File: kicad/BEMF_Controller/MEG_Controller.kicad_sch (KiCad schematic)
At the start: 77 parts, among them J1 HEADER4VALULOK, J2 Recovery, J3 FUSE, J5 Load, J7 Vin, Q1 C3M0280090D, Q2 C3M0280090D, Q3 C3M0280090D, Q4 C3M0280090D, U1 BlackPill_STLINK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

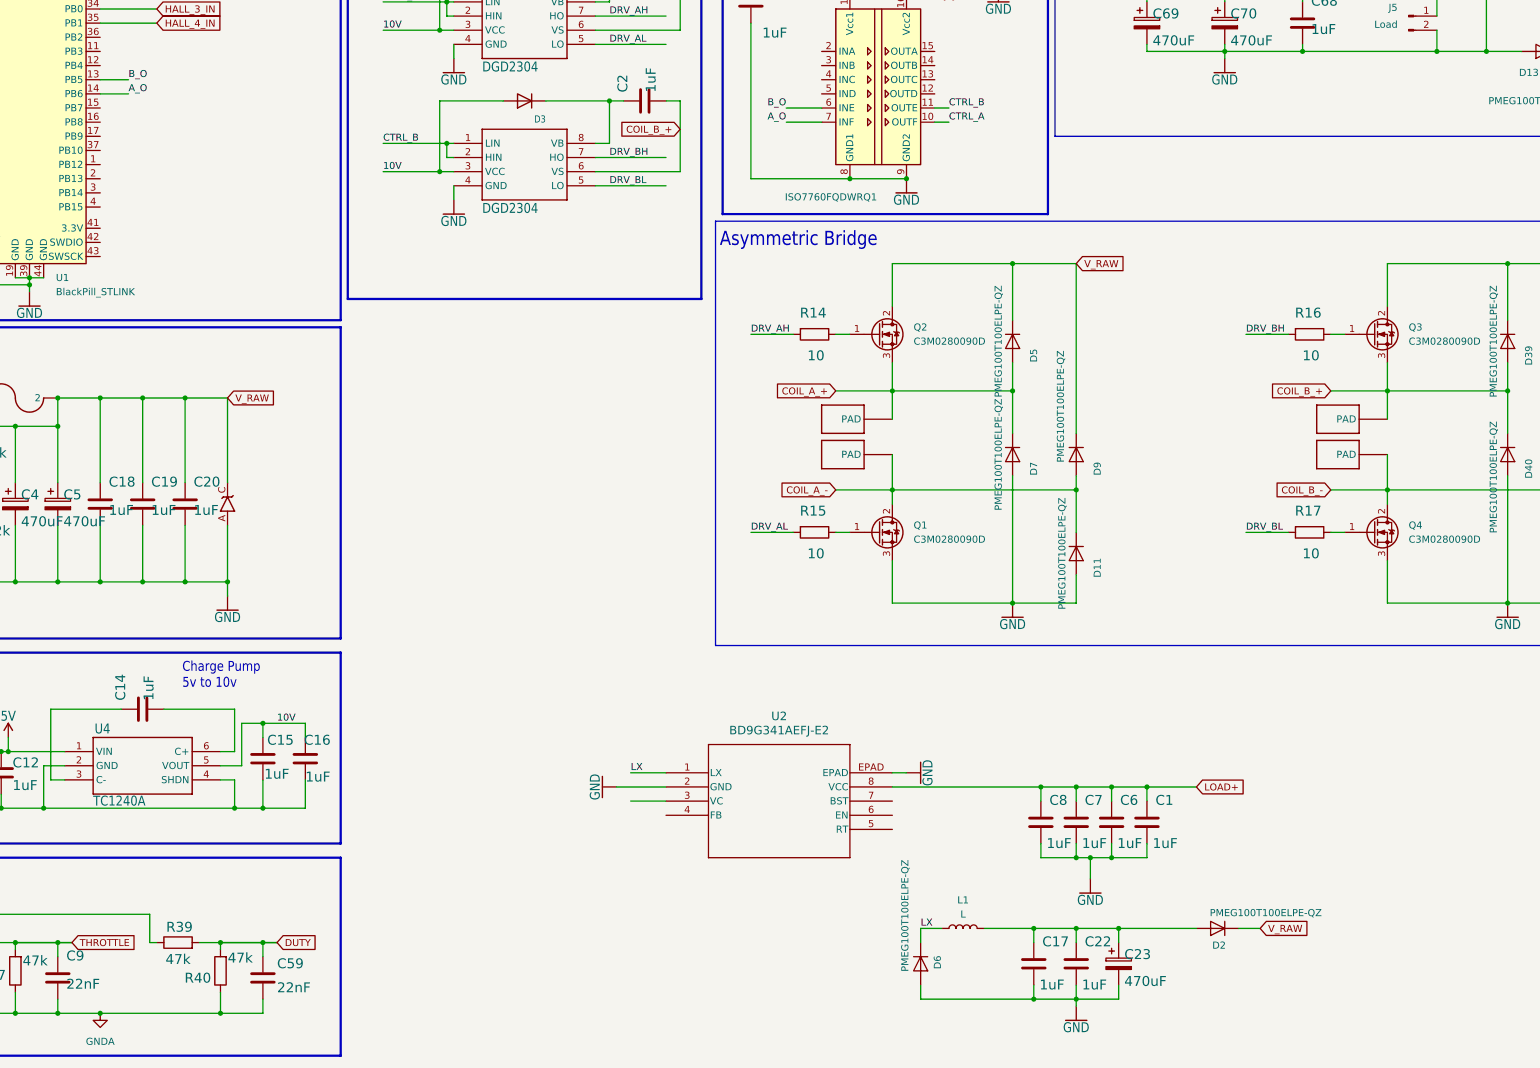
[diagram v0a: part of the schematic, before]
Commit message: Finished buck converter schematic
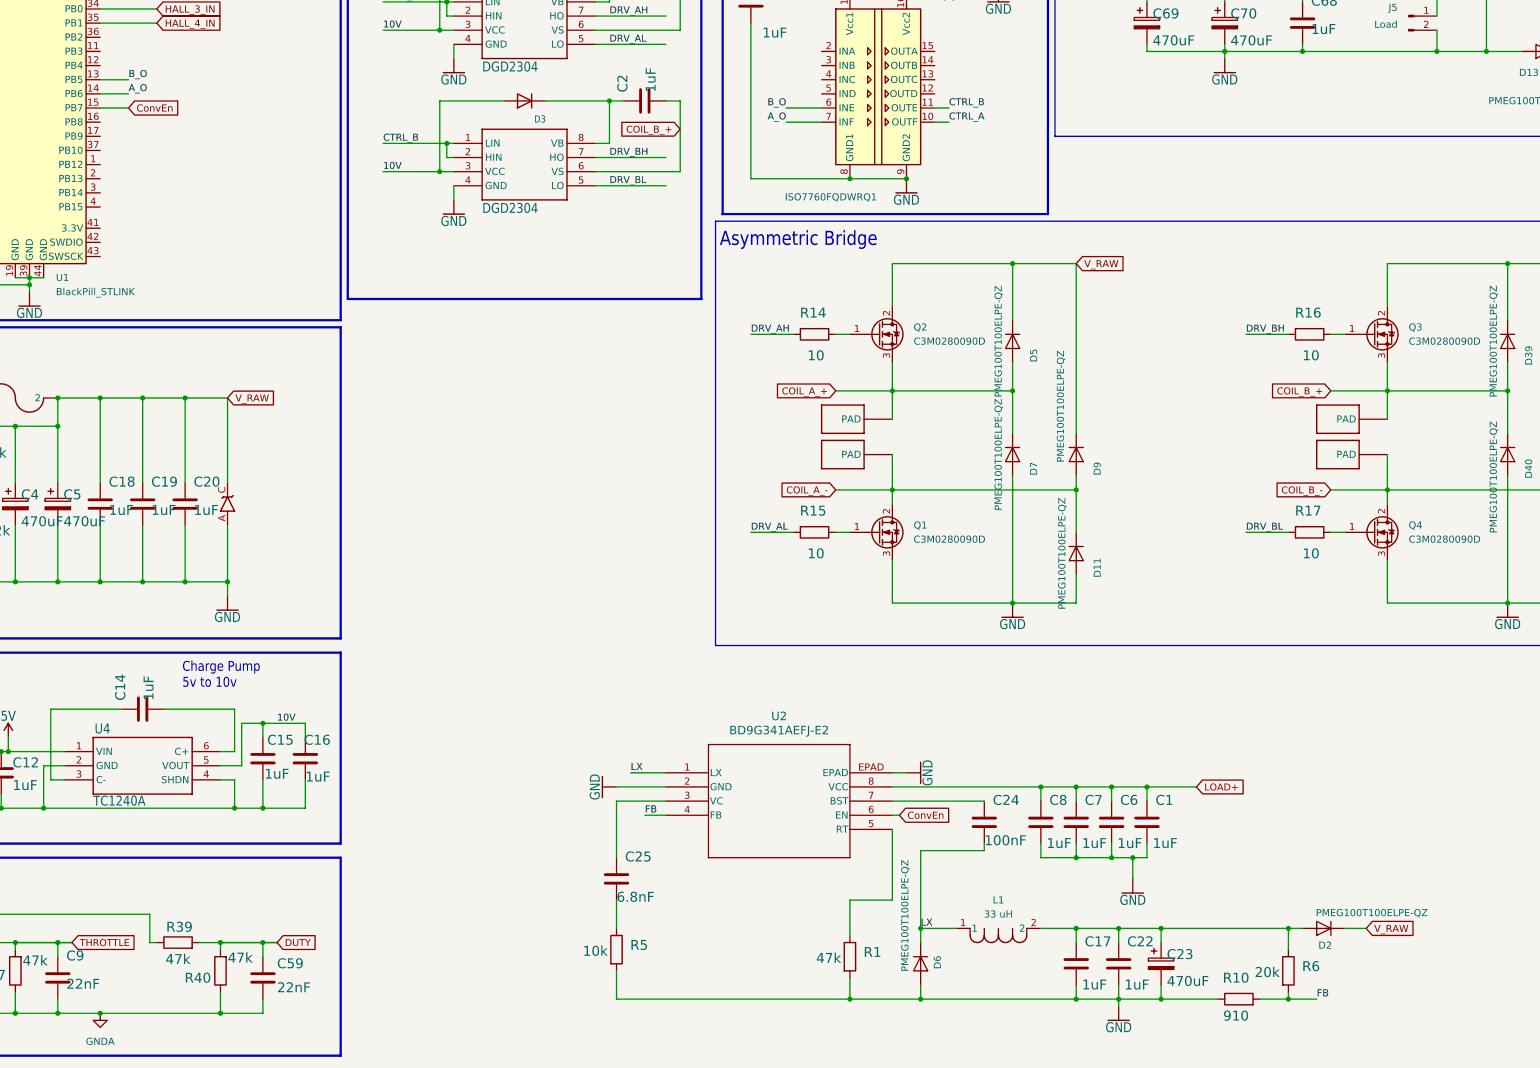
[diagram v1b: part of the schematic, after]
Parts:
- added C24: 100nF, Capacitor_SMD:C_0805_2012Metric, symbol Component_Library:CHV1812N250105MXT
- added C25: 6.8nF, Capacitor_SMD:C_0805_2012Metric, symbol Component_Library:CHV1812N250105MXT
- added R1: 47k, Resistor_SMD:R_1206_3216Metric, symbol Component_Library:R47k
- added R10: 910, Resistor_SMD:R_1206_3216Metric, symbol Component_Library:R47k
- added R5: 10k, Resistor_SMD:R_1206_3216Metric, symbol Component_Library:R47k
- added R6: 20k, Resistor_SMD:R_1206_3216Metric, symbol Component_Library:R47k
- L1: value L -> 33 uH; footprint (none) -> main:IND_BOURNS_SRN1060; symbol Device:L -> Component_Library:33 uH SRN1060-330M
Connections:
- net GND: now also R1.2, R10.1, R5.2
- net LX: now also C24.2
- net at C17.1, C22.1, C23.1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: now also R6.1
- net at U2.3 (VC): now also C25.1
- net FB: now reaches U2.4 (FB)
- net FB: now also R10.2, R6.2
- net at U2.5 (RT): now also R1.1
- net ConvEn: now reaches U2.6 (EN)
- net ConvEn: now also U1.15 (PB7)
- net at U2.7 (BST): now also C24.1
- new net: C25.2, R5.1
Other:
- moved on the sheet: C17, C22, C23, D2

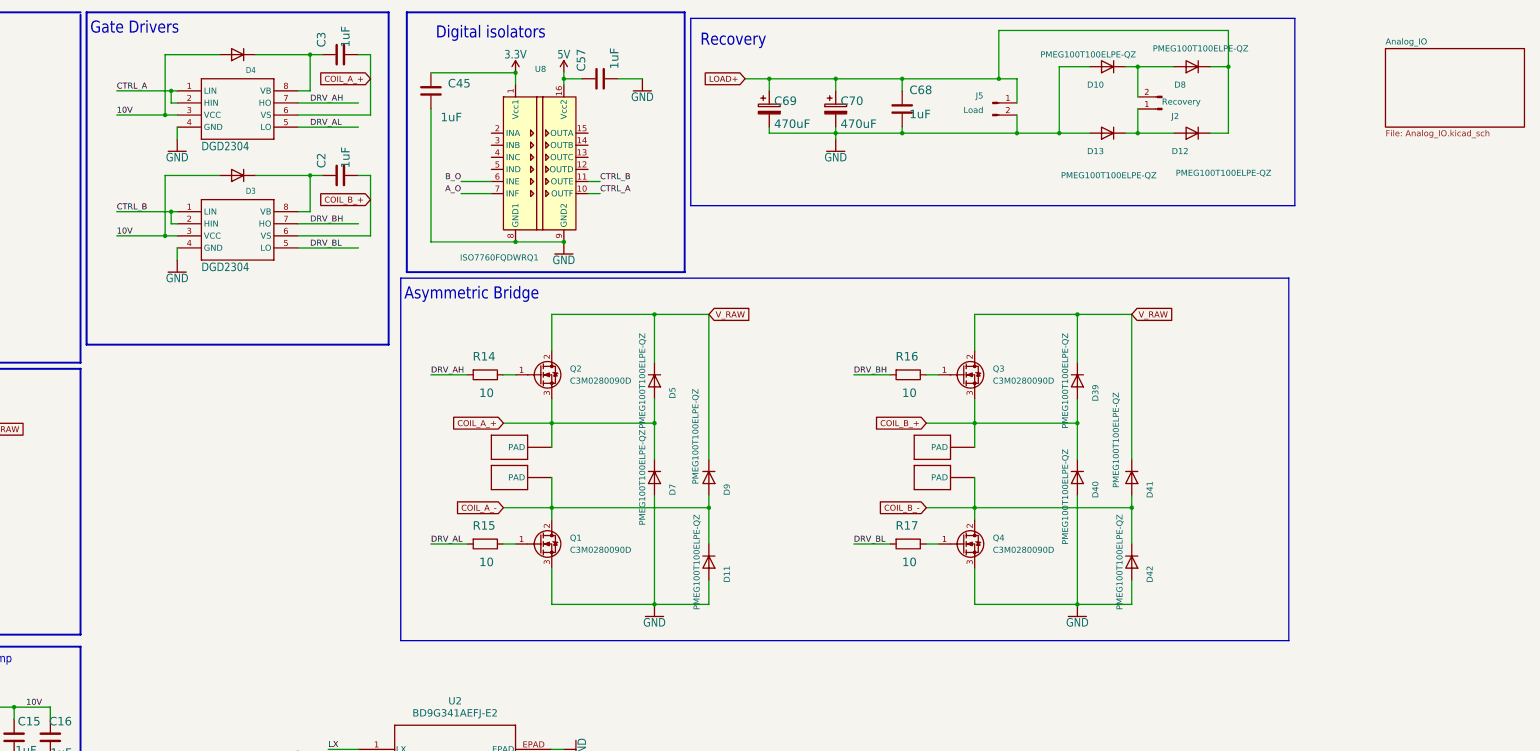
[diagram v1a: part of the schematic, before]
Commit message: Updated gate drivers.
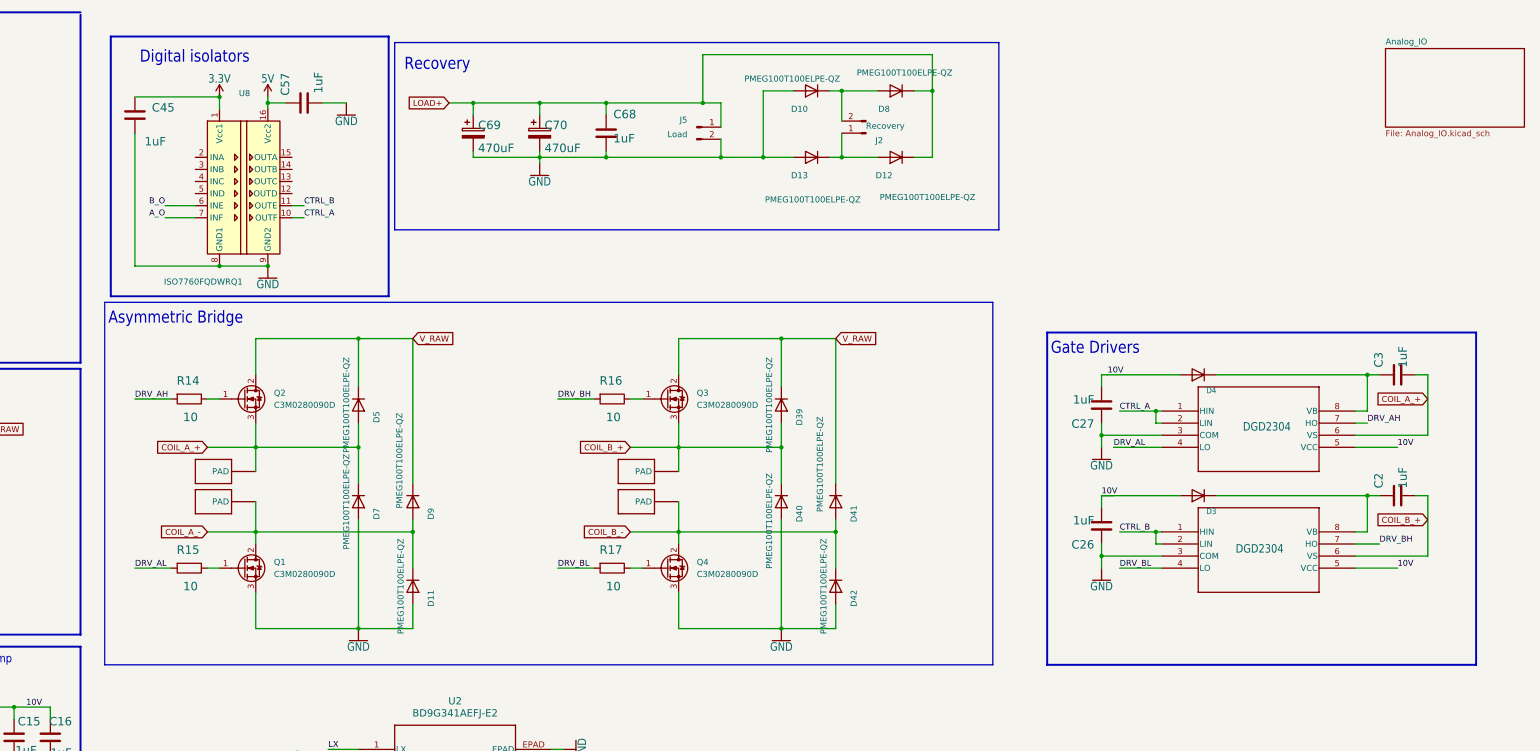
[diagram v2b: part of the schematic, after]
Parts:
- added C26, C27: 1uF, Capacitor_SMD:C_1812_4532Metric, symbol Component_Library:CHV1812N250105MXT
- U5, U6: footprint Package_SO:SOIC-8_3.9x4.9mm_P1.27mm -> main:SOICN-8_LTF; symbol Component_Library:DGD2304 -> Component_Library:LF2190NTR
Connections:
- net 10V: now also U5.5 (VCC), U6.5 (VCC), C26.2, C27.2; no longer U5.3 (VCC), U6.3 (VCC)
- net DRV_AL: now also U5.4 (LO); no longer U5.5 (LO)
- net DRV_BL: now also U6.4 (LO); no longer U6.5 (LO)
- net GND: now also U5.3 (COM), U6.3 (COM), C26.1, C27.1; no longer U5.4 (GND), U6.4 (GND)
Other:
- moved on the sheet: C2, C3, C45, C57, C68, C69, C70, D10, D11, D12, D13, D3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

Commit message: Pretty much complete, but a few things left to do.
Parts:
- removed C14: 1uF, Capacitor_SMD:C_1812_4532Metric, symbol Component_Library:CHV1812N250105MXT
- removed U$1: COIL_A+, main:PAD, symbol main-eagle-import:PAD
- removed U$2, U$3, U$4, U$5, U$6: PAD, main:PAD, symbol main-eagle-import:PAD
- removed U4: TC1240A, main:SOT23-6, symbol main-eagle-import:TC1240A
- added C14, C28: 470uF, Capacitor_THT:CP_Radial_D10.0mm_P5.00mm, symbol Component_Library:C_Pol_470uF
- added C30: 1uF, Capacitor_SMD:C_1812_4532Metric, symbol Component_Library:CHV1812N250105MXT
- added J6: Coil_B, TerminalBlock_Phoenix:TerminalBlock_Phoenix_MKDS-1,5-2-5.08_1x02_P5.08mm_Horizontal, symbol Connector:Conn_01x02_Pin
- added J8: Coil_A, TerminalBlock_Phoenix:TerminalBlock_Phoenix_MKDS-1,5-2-5.08_1x02_P5.08mm_Horizontal, symbol Connector:Conn_01x02_Pin
- added J9: Vpower, TerminalBlock_Phoenix:TerminalBlock_Phoenix_MKDS-1,5-2-5.08_1x02_P5.08mm_Horizontal, symbol Connector:Conn_01x02_Pin
- added U4: V_REG_7810, main:V78W_BACKWARDS, symbol main-eagle-import:V_REG_78XX
- J1: footprint main:4PINVALULOK -> TerminalBlock_Phoenix:TerminalBlock_Phoenix_MKDS-1,5-4-5.08_1x04_P5.08mm_Horizontal
- Q1, Q2, Q3, Q4: footprint Package_TO_SOT_THT:TO-247-3_Horizontal_TabDown -> Package_TO_SOT_THT:TO-247-3_Vertical; symbol Component_Library:C3M0280090D_TO247 -> Component_Library:C3M0280090D_TO247-Vertical
- R14, R15, R16, R17: value 10 -> 2R2; footprint Resistor_THT:R_Axial_DIN0411_L9.9mm_D3.6mm_P15.24mm_Horizontal -> Resistor_SMD:R_1206_3216Metric; symbol Component_Library:ROX1SJ10R -> Component_Library:2R2
- U3: value V_REG_78XX -> V_REG_7805
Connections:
- net 3.3V: now also C30.1
- net 5V: now also C16.1, C14.1
- net A_O: now also U1.17 (PB9); no longer U1.14 (PB6)
- net B_O: now also U1.16 (PB8); no longer U1.13 (PB5)
- net COIL_A_+: now also J8.2 (Pin_2)
- net COIL_A_-: now also J8.1 (Pin_1)
- net COIL_B_+: now also J6.2 (Pin_2)
- net COIL_B_-: now also J6.1 (Pin_1)
- net ConvEn: now also U1.24 (PC15), U8.5 (IND); no longer U1.15 (PB7), U2.6 (EN)
- net DUTY: now also U1.33 (PA7); no longer U1.28 (PA2)
- net GND: now also C14.2, C28.2, C30.2, J9.2 (Pin_2), U4.GND
- net HALL_1_IN: now also U1.28 (PA2); no longer U1.32 (PA6)
- net HALL_2_IN: now also U1.29 (PA3); no longer U1.33 (PA7)
- net HALL_3_IN: now also U1.30 (PA4); no longer U1.34 (PB0)
- net HALL_4_IN: now also U1.31 (PA5); no longer U1.35 (PB1)
- net THROTTLE: now also U1.32 (PA6); no longer U1.29 (PA3)
- net REC_B: now reaches D12.3 (K), D13.1 (A), D13.2 (A), J2.1 (Pin_1)
- net at J7.1 (Pin_1), JP7.2 (B), U3.IN: now also U4.IN
- net REC_A: now reaches D10.1 (A), D10.2 (A), D8.3 (K), J2.2 (Pin_2)
- net ConvEnIso: now reaches U8.12 (OUTD)
- net ConvEnIso: now also U2.6 (EN)
- net at J3.1A (1), J3.1B (1): now also J9.1 (Pin_1)
- net 10V renamed +10V
- net +10V: now also C28.1, U4.OUT; no longer C16.1
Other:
- note added: "Linear Regulator 60-9v to 5v"
- note added: "Regulator 10V"
- note removed: "Buck Regulator 60-9v to 5v"
- note removed: "Charge Pump 5v to 10v"
- moved on the sheet: C15
